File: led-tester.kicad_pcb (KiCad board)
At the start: 2 copper layers, 60.2 x 79.2 mm, 41 parts, among them J1 V_In, SW1 PWR_SW

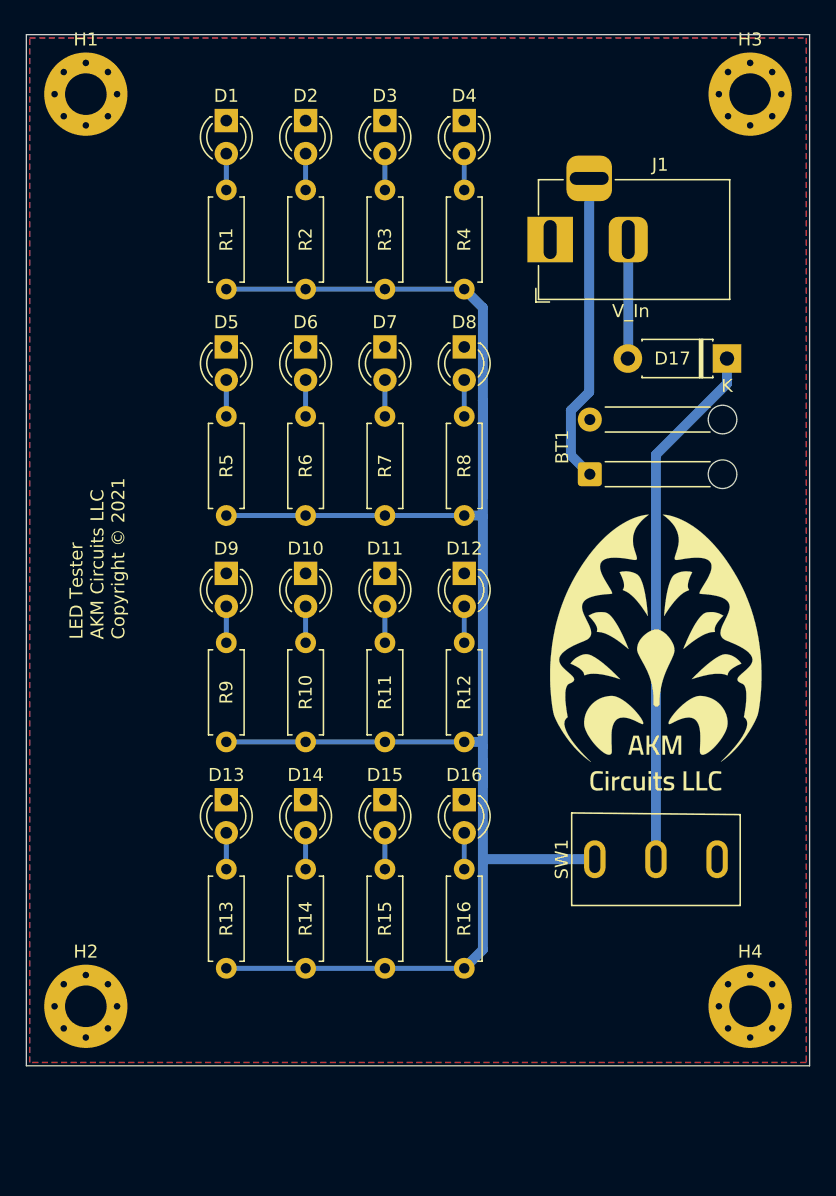
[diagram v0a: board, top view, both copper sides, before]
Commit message: add finalized draft schematic and pcb layout
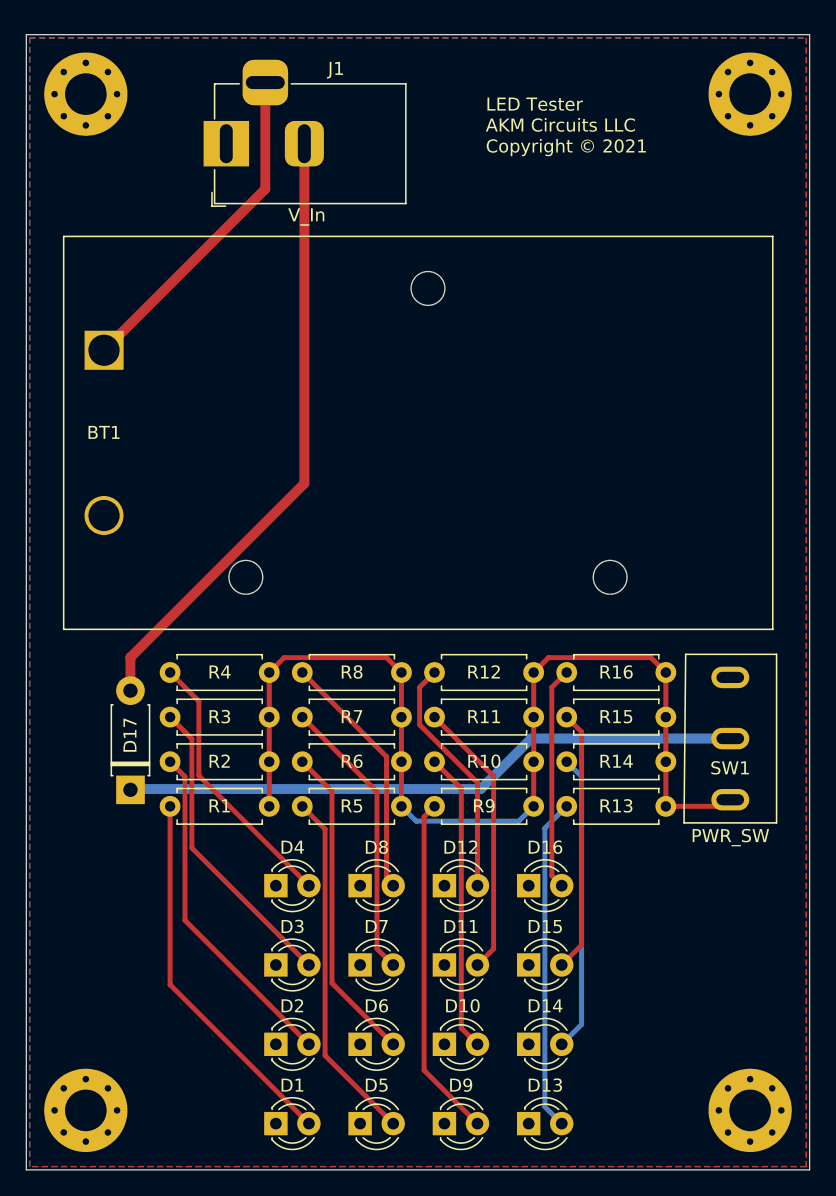
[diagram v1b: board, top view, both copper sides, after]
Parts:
- BT1: footprint Connector_Wire:SolderWire-0.25sqmm_1x02_P4.2mm_D0.65mm_OD1.7mm_Relief -> Battery:BatteryHolder_Eagle_12BH611-GR
- SYM1: footprint AKM_Circuits:Logo_2400 -> AKM_Circuits:Logo_800; moved to B.Cu
- moved D1 77.2 mm to (129.3, 142.4), turned to 0 degrees
- moved D2 71.0 mm to (129.3, 136.3), turned to 0 degrees
- moved D3 65.4 mm to (129.3, 130.2), turned to 0 degrees
- moved D5 60.6 mm to (135.8, 142.4), turned to 0 degrees
- moved D4 60.6 mm to (129.3, 124.1), turned to 0 degrees
- moved D17 56.6 mm to (118.1, 116.7), turned to 90 degrees
- moved D6 53.8 mm to (135.8, 136.3), turned to 0 degrees
- moved R1 47.6 mm to (121.2, 118.0), turned to 0 degrees
- moved D7 47.5 mm to (135.8, 130.2), turned to 0 degrees
- moved D9 45.5 mm to (142.2, 142.4), turned to 0 degrees
- moved R2 45.2 mm to (121.2, 114.6), turned to 0 degrees
- moved R3 43.7 mm to (121.2, 111.1), turned to 0 degrees
- moved R4 43.4 mm to (121.2, 107.7), turned to 0 degrees
- moved D8 42.2 mm to (135.8, 124.1), turned to 0 degrees
- moved BT1 38.5 mm to (116.1, 82.9), turned to 180 degrees
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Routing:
- net VCC: track 147.0 -> 79.6 mm
- net Net-(D17-Pad2): track 9.20 -> 47.6 mm
- net Net-(D1-Pad2): track 2.79 -> 28.8 mm
- net Net-(D5-Pad2): track 2.79 -> 27.3 mm
- net Net-(D9-Pad2): track 2.79 -> 26.4 mm
- net Net-(D2-Pad2): track 2.79 -> 26.1 mm
- net Net-(D13-Pad2): track 2.79 -> 25.6 mm
- net Net-(D6-Pad2): track 2.79 -> 24.6 mm
- net Net-(D3-Pad2): track 2.79 -> 23.5 mm
- net Net-(D10-Pad2): track 2.79 -> 23.1 mm
- net Net-(D14-Pad2): track 2.79 -> 22.8 mm
- net Net-(D7-Pad2): track 2.79 -> 21.9 mm
- net Net-(D11-Pad2): track 2.79 -> 21.4 mm
- net Net-(D4-Pad2): track 2.79 -> 20.8 mm
- net Net-(D15-Pad2): track 2.79 -> 20.2 mm
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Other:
- board size 60.2 x 79.2 mm -> 60.2 x 87.2 mm

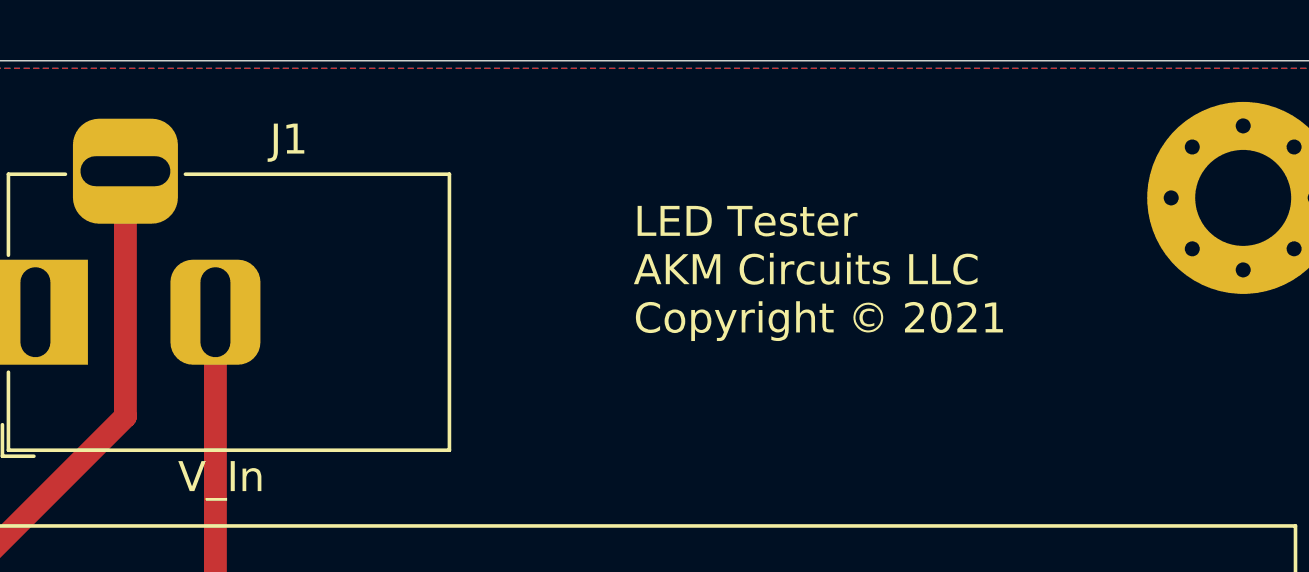
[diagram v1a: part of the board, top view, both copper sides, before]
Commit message: adjust silkscreen placement
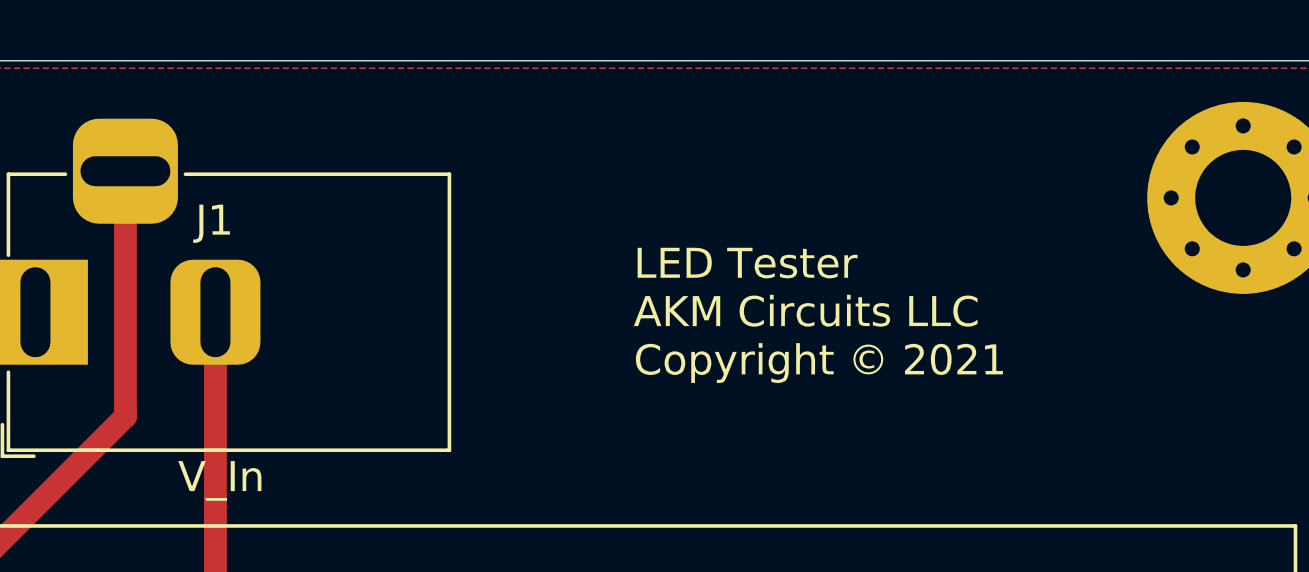
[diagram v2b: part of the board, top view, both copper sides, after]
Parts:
- moved SYM1 0.65 mm to (140.3, 102.4)
